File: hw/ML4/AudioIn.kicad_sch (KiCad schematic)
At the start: 24 parts, among them T2 Transformer_1P_1S, U1 LMV324 (Actually LTV9161), U5 LTV-356T

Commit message: Updates for ML4
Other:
- note added: "1.44V"
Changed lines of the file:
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@@
+		)
+	)
+	(text "1.44V"
+		(exclude_from_sim no)
+		(at 247.142 56.896 0)
+		(effects
+			(font
+				(size 1.27 1.27)
+				(thickness 0.254)
+				(bold yes)
+				(color 140 18 255 1)
+			)
 		)
 	)
@@
 		)
 	)
+	(text "1.44V"
+		(exclude_from_sim no)
+		(at 163.068 53.848 0)
+		(effects
+			(font
+				(size 1.27 1.27)
+				(thickness 0.254)
+				(bold yes)
+				(color 140 18 255 1)
+			)
+		)
+	)
 	(text "Anti-Aliasing LPF Filter\nfc = 4kHz"
 		(exclude_from_sim no)
@@
 		)
 	)
+	(text "1.44V"
+		(exclude_from_sim no)
+		(at 105.41 64.262 0)
+		(effects
+			(font
+				(size 1.27 1.27)
+				(thickness 0.254)
+				(bold yes)
+				(color 140 18 255 1)
+			)
+		)
+	)

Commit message: Working on JCSC BOM
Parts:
- R10: LCSC (none) -> C17629
- R11: LCSC (none) -> C17589
- R15: LCSC (none) -> C4310
- R16: LCSC (none) -> C17530
- R18, R26: LCSC (none) -> C17477
- R19: LCSC (none) -> C17557
- R9: LCSC (none) -> C17513

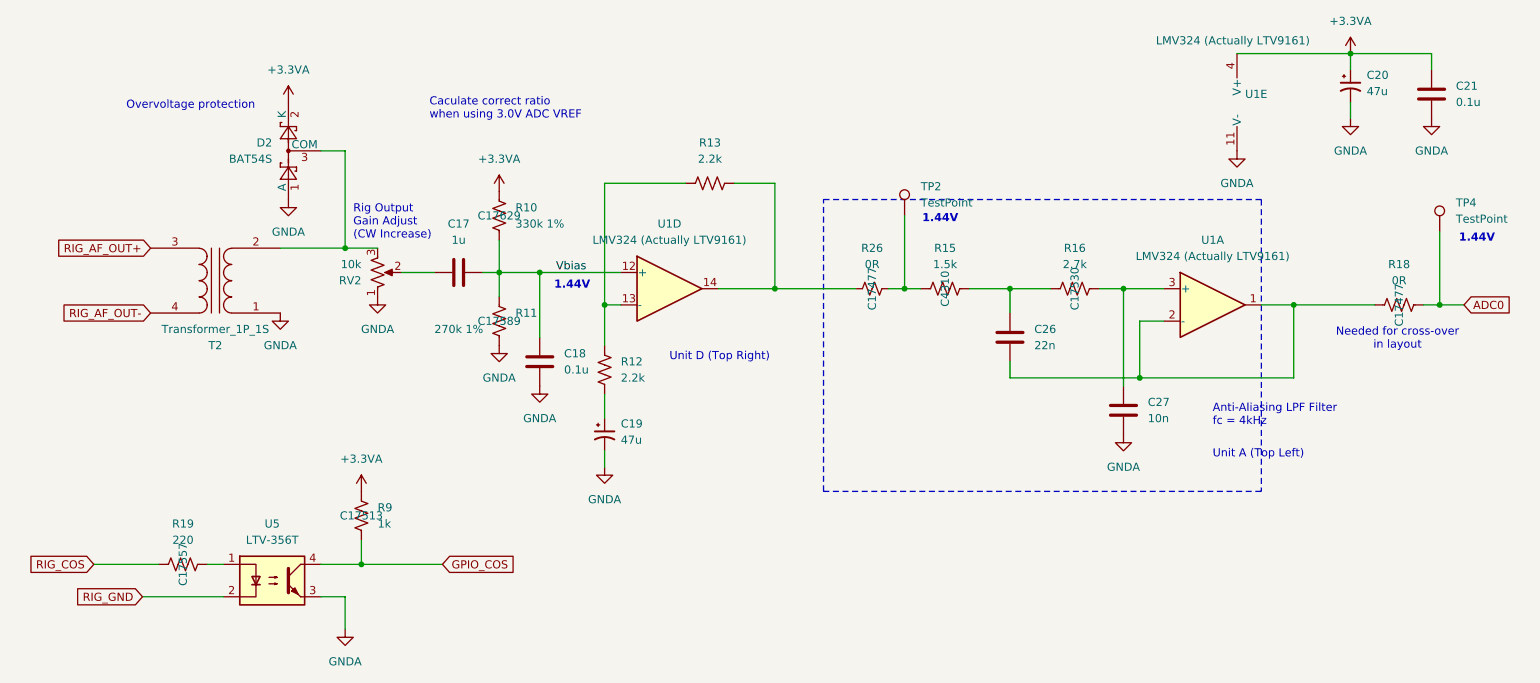
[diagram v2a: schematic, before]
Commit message: Working on adding LCSC part numbers
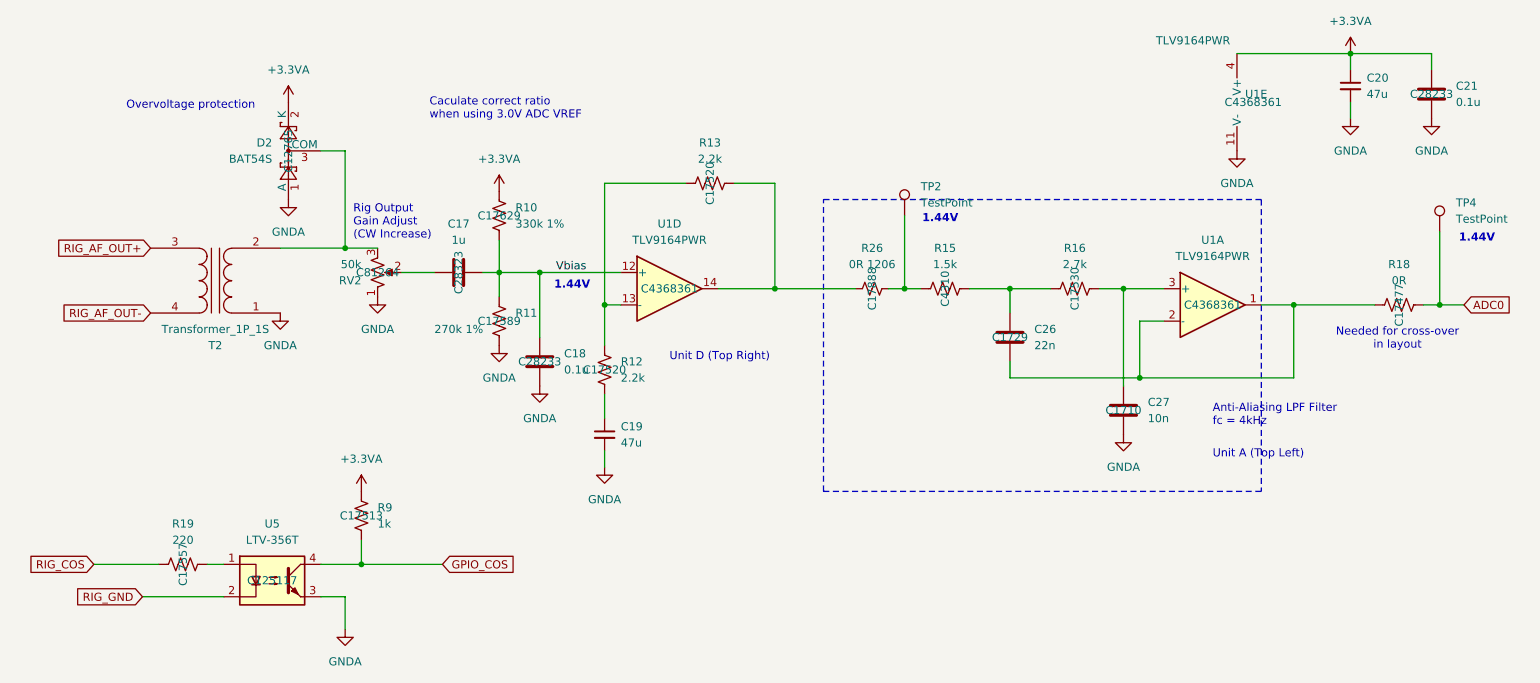
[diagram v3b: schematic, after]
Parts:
- removed C19, C20: 47u, bruce-footprints:CPOL_0805_2012Metric_Pad1.18x1.45mm_HandSolder, symbol Device:C_Polarized_Small_US
- added C19, C20: 47u, Capacitor_SMD:C_0805_2012Metric_Pad1.18x1.45mm_HandSolder, symbol Device:C_Small
- C17: LCSC (none) -> C28323
- C18, C21: LCSC (none) -> C28233
- C26: LCSC (none) -> C1729
- C27: LCSC (none) -> C1710
- D2: LCSC (none) -> C12765
- R12, R13: LCSC (none) -> C17520
- R26: value 0R -> 0R 1206; LCSC C17477 -> C17888
- RV2: value 10k -> 50k; LCSC (none) -> C81264
- U1: value LMV324 (Actually LTV9161) -> TLV9164PWR; LCSC (none) -> C4368361
- U5: LCSC (none) -> C125117
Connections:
- net +3.3VA: now also C20.1
- net GNDA: now also C19.2, C20.2
- net at R12.1: now also C19.1

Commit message: Working on adding LCSC part numbers
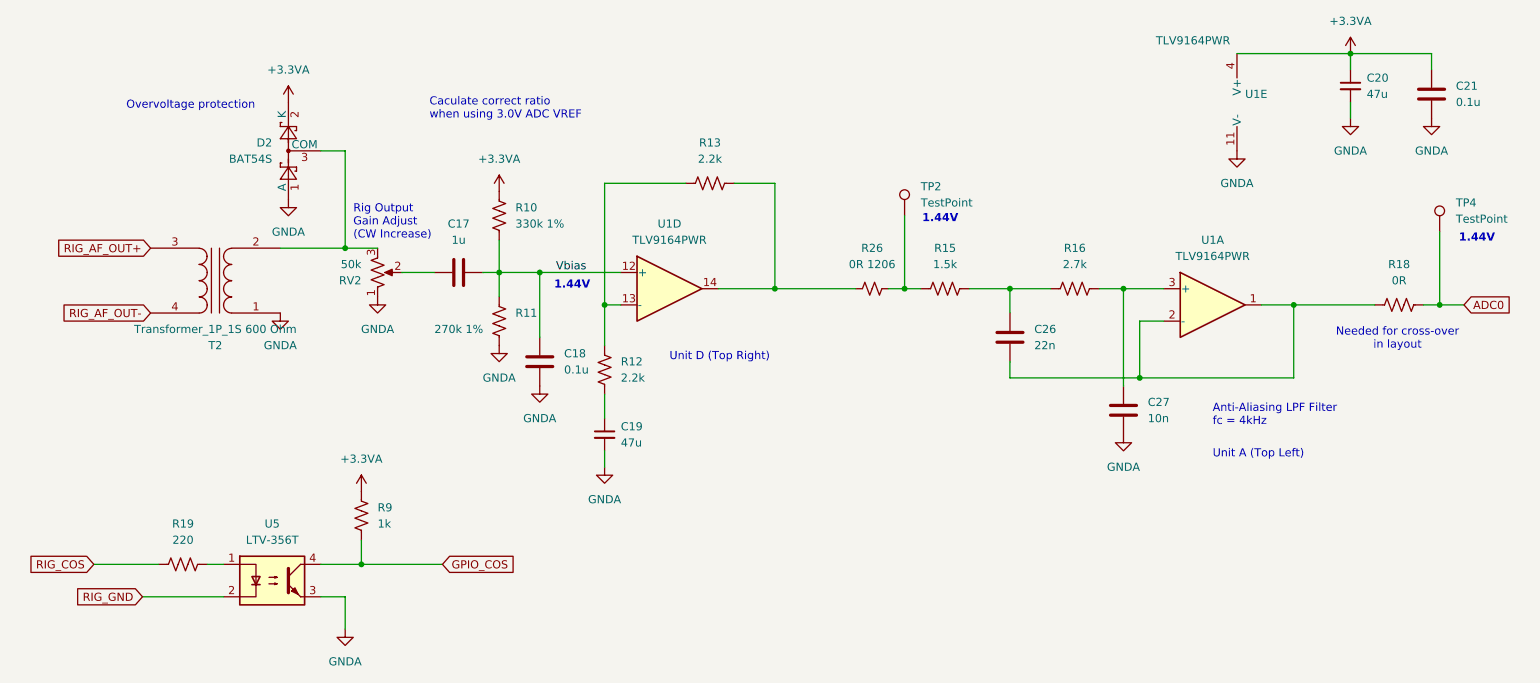
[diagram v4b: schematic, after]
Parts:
- T2: value Transformer_1P_1S -> Transformer_1P_1S 600 Ohm
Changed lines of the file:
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@@
 		(comment 1 "Copyright (C) 2024 - Not For Commercial Use")
 	)
-	(rectangle
-		(start 144.78 50.8)
-		(end 213.36 96.52)
-		(stroke
-			(width 0)
-			(type dot)
-			(color 255 55 72 1)
-		)
-		(fill
-			(type none)
-		)
-	)
 	(text "Rig Output \nGain Adjust\n(CW Increase)"
 		(exclude_from_sim no)
@@
 					(size 1.27 1.27)
 				)
+				(hide yes)
 			)
 		)
@@
 					(size 1.27 1.27)
 				)
+				(hide yes)
 			)
 		)
@@
 					(size 1.27 1.27)
 				)
+				(hide yes)
 			)
 		)
@@
 					(size 1.27 1.27)
 				)
+				(hide yes)
 			)
 		)
@@
 					(size 1.27 1.27)
 				)
+				(hide yes)
 			)
 		)
@@
 					(size 1.27 1.27)
 				)
+				(hide yes)
 			)
 		)
@@
 					(size 1.27 1.27)
 				)
+				(hide yes)
 			)
 		)
@@
 					(size 1.27 1.27)
 				)
+				(hide yes)
 			)
 		)
@@
 					(size 1.27 1.27)
 				)
+				(hide yes)
 			)
 		)
@@
 					(size 1.27 1.27)
 				)
+				(hide yes)
 			)
 		)
@@
 					(size 1.27 1.27)
 				)
+				(hide yes)
 			)
 		)
@@
 					(size 1.27 1.27)
 				)
+				(hide yes)
 			)
 		)
@@
 					(size 1.27 1.27)
 				)
+				(hide yes)
 			)
 		)
@@
 			)
 		)
-		(property "Value" "Transformer_1P_1S"
+		(property "Value" "Transformer_1P_1S 600 Ohm"
 			(at 49.5173 71.12 0)
 			(effects
@@
 					(size 1.27 1.27)
 				)
+				(hide yes)
 			)
 		)
@@
 					(size 1.27 1.27)
 				)
+				(hide yes)
 			)
 		)
@@
 					(size 1.27 1.27)
 				)
+				(hide yes)
 			)
 		)
@@
 					(size 1.27 1.27)
 				)
+				(hide yes)
 			)
 		)
@@
 					(size 1.27 1.27)
 				)
+				(hide yes)
 			)
 		)
@@
 					(size 1.27 1.27)
 				)
+				(hide yes)
 			)
 		)
@@
 					(size 1.27 1.27)
 				)
+				(hide yes)
 			)
 		)
@@
 					(size 1.27 1.27)
 				)
+				(hide yes)
 			)
 		)

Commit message: Working on adding LCSC part numbers
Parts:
- T2: BOM Comments (none) -> 600:600 ohm audio transformer (Amazon or AliExpress)
- TP2, TP4: BOM Comments (none) -> No component, PCB test point; now left out of the parts list
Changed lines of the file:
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@@
 		(unit 1)
 		(exclude_from_sim no)
-		(in_bom yes)
+		(in_bom no)
 		(on_board yes)
 		(dnp no)
@@
 					(size 1.27 1.27)
 				)
+			)
+		)
+		(property "BOM Comments" "No component, PCB test point"
+			(at 241.3 55.88 0)
+			(effects
+				(font
+					(size 1.27 1.27)
+				)
+				(hide yes)
+			)
+		)
+		(property "DK" ""
+			(at 241.3 55.88 0)
+			(effects
+				(font
+					(size 1.27 1.27)
+				)
+				(hide yes)
 			)
 		)
@@
 			)
 		)
+		(property "BOM Comments" "600:600 ohm audio transformer (Amazon or AliExpress)"
+			(at 49.53 63.5 0)
+			(effects
+				(font
+					(size 1.27 1.27)
+				)
+				(hide yes)
+			)
+		)
 		(pin "3"
 		)
@@
 		(unit 1)
 		(exclude_from_sim no)
-		(in_bom yes)
+		(in_bom no)
 		(on_board yes)
 		(dnp no)
@@
 			)
 		)
+		(property "BOM Comments" "No component, PCB test point"
+			(at 157.48 53.34 0)
+			(effects
+				(font
+					(size 1.27 1.27)
+				)
+				(hide yes)
+			)
+		)
+		(property "DK" ""
+			(at 157.48 53.34 0)
+			(effects
+				(font
+					(size 1.27 1.27)
+				)
+				(hide yes)
+			)
+		)

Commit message: Working on ML4
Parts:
- removed T2: Transformer_1P_1S 600 Ohm, bruce-footprints:CheapAudioTransformer, symbol Device:Transformer_1P_1S
- added TR2: SM-LP-5001, bruce-footprints:TRAN6_SM-LP-5001_BRN, symbol symbol-library-1:SM-LP-5001
- C17: value 1u -> 47u; LCSC C28323 -> C16780
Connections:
- net GNDA: now also TR2.4
- net RIG_AF_OUT+: now also TR2.1
- net RIG_AF_OUT-: now also TR2.3
- net at D2.3 (COM), RV2.3: now also TR2.6
- no-connect marks 0 -> 2
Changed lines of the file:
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@@
 		(color 0 0 0 0)
 	)
+	(no_connect
+		(at 44.45 63.5)
+	)
+	(no_connect
+		(at 54.61 63.5)
+	)
 	(wire
 		(pts
@@
 	(wire
 		(pts
+			(xy 39.37 68.58) (xy 44.45 68.58)
+		)
+		(stroke
+			(width 0)
+			(type default)
+		)
+	)
+	(wire
+		(pts
 			(xy 93.98 62.23) (xy 93.98 66.04)
 		)
@@
 	(wire
 		(pts
-			(xy 59.69 58.42) (xy 69.85 58.42)
-		)
-		(stroke
-			(width 0)
-			(type default)
-		)
-	)
-	(wire
-		(pts
 			(xy 66.04 107.95) (xy 72.39 107.95)
 		)
@@
 	(wire
 		(pts
+			(xy 54.61 58.42) (xy 69.85 58.42)
+		)
+		(stroke
+			(width 0)
+			(type default)
+		)
+	)
+	(wire
+		(pts
 			(xy 154.94 64.77) (xy 157.48 64.77)
 		)
@@
 	(wire
 		(pts
+			(xy 39.37 58.42) (xy 44.45 58.42)
+		)
+		(stroke
+			(width 0)
+			(type default)
+		)
+	)
+	(wire
+		(pts
 			(xy 100.33 62.23) (xy 100.33 72.39)
 		)
@@
 		(pts
 			(xy 69.85 43.18) (xy 69.85 58.42)
+		)
+		(stroke
+			(width 0)
+			(type default)
+		)
+	)
+	(wire
+		(pts
+			(xy 54.61 68.58) (xy 59.69 68.58)
 		)
 		(stroke
@@
 	)
 	(symbol
+		(lib_id "symbol-library-1:SM-LP-5001")
+		(at 49.53 63.5 0)
+		(unit 1)
+		(exclude_from_sim no)
+		(in_bom yes)
+		(on_board yes)
+		(dnp no)
+		(fields_autoplaced yes)
+		(property "Reference" "TR2"
+			(at 49.53 53.34 0)
+			(effects
+				(font
+					(size 1.27 1.27)
+				)
+			)
+		)
+		(property "Value" "SM-LP-5001"
+			(at 49.53 55.88 0)
+			(effects
+				(font
+					(size 1.27 1.27)
+				)
+			)
+		)
+		(property "Footprint" "bruce-footprints:TRAN6_SM-LP-5001_BRN"
+			(at 49.53 63.5 0)
+			(effects
+				(font
+					(size 1.27 1.27)
+				)
+				(hide yes)
+			)
+		)
+		(property "Datasheet" "https://www.bourns.com/docs/Product-Datasheets/SMLP5001.pdf"
+			(at 49.53 63.5 0)
+			(effects
+				(font
+					(size 1.27 1.27)
+				)
+				(hide yes)
+			)
+		)
+		(property "Description" "Bourns Audio Transformer 1:1 Center Tap"
+			(at 49.53 63.5 0)
+			(effects
+				(font
+					(size 1.27 1.27)
+				)
+				(hide yes)
+			)
+		)
+		(property "LCSC" "C7503474"
+			(at 49.53 63.5 0)
+			(effects
+				(font
+					(size 1.27 1.27)
+				)
+				(hide yes)
+			)
+		)
+		(pin "1"
+		)
+		(pin "5"
+		)
+		(pin "4"
+		)
+		(pin "3"
+		)
+		(pin "6"
+		)
+		(pin "2"
+		)
+		(instances
+			(project ""
+				(path "/5f8f636b-fd0e-498e-8696-0a023acb4c09/605cddf5-737f-47be-b5fd-7ed3decef4e0"
+					(reference "TR2")
+					(unit 1)
+				)
+			)
+		)
+	)
+	(symbol
 		(lib_id "Device:R_US")
 		(at 234.95 67.31 90)
@@
 			)
 		)
-		(property "Value" "1u"
+		(property "Value" "47u"
 			(at 87.63 57.15 90)
 			(effects
@@
 			)
 		)
-		(property "LCSC" "C28323 "
+		(property "LCSC" "C16780 "
+			(at 87.63 62.23 0)
+			(effects
+				(font
+					(size 1.27 1.27)
+				)
+				(hide yes)
+			)
+		)
+		(property "DK" ""
+			(at 87.63 62.23 0)
+			(effects
+				(font
+					(size 1.27 1.27)
+				)
+				(hide yes)
+			)
+		)
+		(property "BOM Comments" ""
 			(at 87.63 62.23 0)
 			(effects
@@
 					(unit 1)
 				)
-			)
-		)
-	)
-	(symbol
-		(lib_id "Device:Transformer_1P_1S")
-		(at 49.53 63.5 180)
-		(unit 1)
-		(exclude_from_sim no)
-		(in_bom yes)
-		(on_board yes)
-		(dnp no)
-		(property "Reference" "T2"
-			(at 49.5173 73.66 0)
-			(effects
-				(font
-					(size 1.27 1.27)
-				)
-			)
-		)
-		(property "Value" "Transformer_1P_1S 600 Ohm"
-			(at 49.5173 71.12 0)
-			(effects
-				(font
-					(size 1.27 1.27)
-				)
-			)
-		)
-		(property "Footprint" "bruce-footprints:CheapAudioTransformer"
-			(at 49.53 63.5 0)
-			(effects
-				(font
-					(size 1.27 1.27)
-				)
-				(hide yes)
-			)
-		)
-		(property "Datasheet" "~"
-			(at 49.53 63.5 0)
-			(effects
-				(font
-					(size 1.27 1.27)
-				)
-				(hide yes)
-			)
-		)
-		(property "Description" "Transformer, single primary, single secondary"
-			(at 49.53 63.5 0)
-			(effects
-				(font
-					(size 1.27 1.27)
-				)
-				(hide yes)
-			)
-		)
-		(property "LCSC" ""
-			(at 49.53 63.5 0)
-			(effects
-				(font
-					(size 1.27 1.27)
-				)
-			)
-		)
-		(property "BOM Comments" "600:600 ohm audio transformer (Amazon or AliExpress)"
-			(at 49.53 63.5 0)
-			(effects
-				(font
-					(size 1.27 1.27)
-				)
-				(hide yes)
-			)
-		)
-		(pin "3"
-		)
-		(pin "4"
-		)
-		(pin "2"
-		)
-		(pin "1"
-		)
-		(instances
-			(project "ML4"
-				(path "/5f8f636b-fd0e-498e-8696-0a023acb4c09/605cddf5-737f-47be-b5fd-7ed3decef4e0"
-					(reference "T2")
-					(unit 1)
-				)
